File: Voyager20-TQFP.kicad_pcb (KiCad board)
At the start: 2 copper layers, 73 x 95.2 mm, 92 parts, among them Q1 Q_NPN_BEC, SW1 SW_Push, U1 ATmega32U2-AU, U2 PRTR5V0U2X, Y1 16MHz

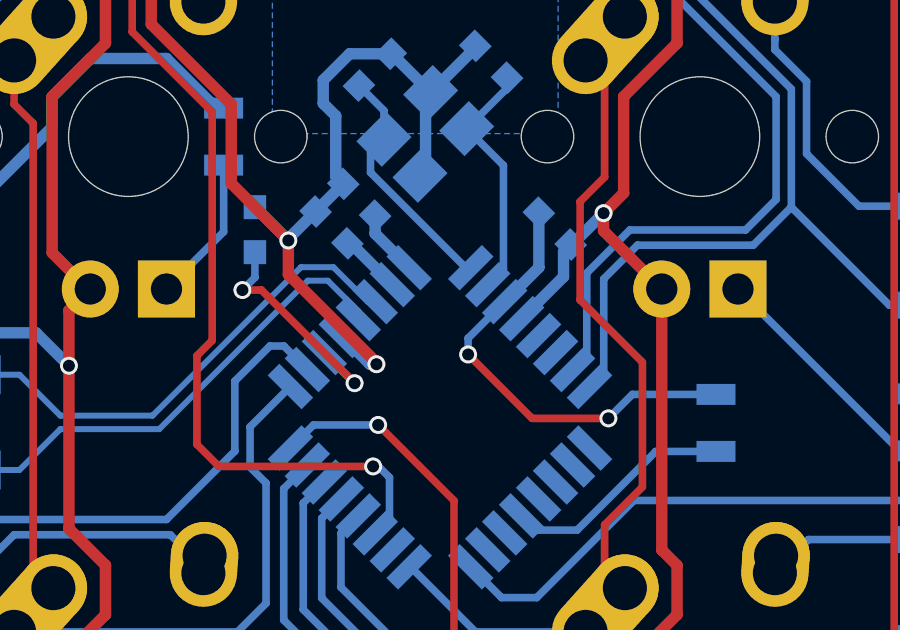
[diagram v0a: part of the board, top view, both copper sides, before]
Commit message: fixed +5v and GND lol
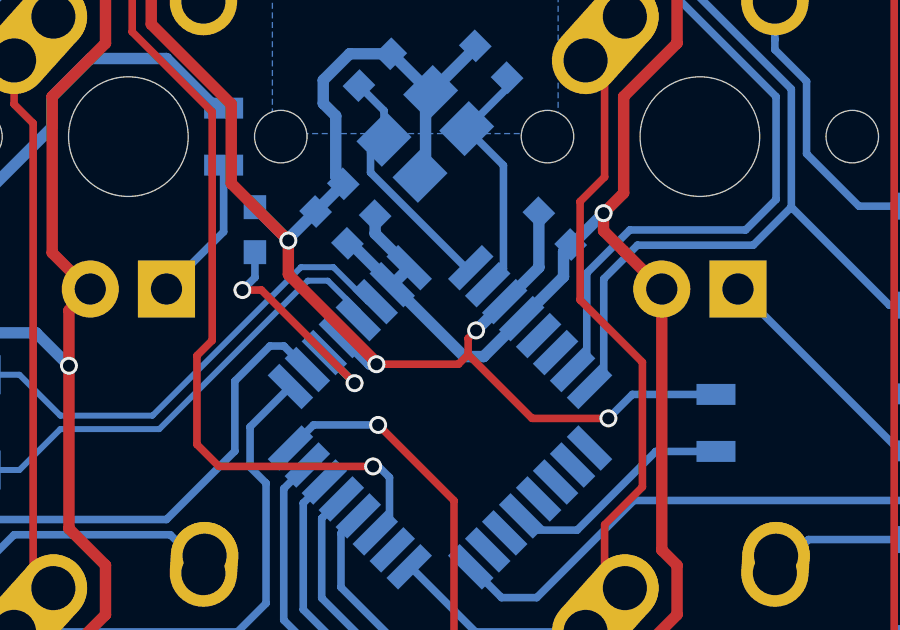
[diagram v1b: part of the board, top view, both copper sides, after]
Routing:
- net +5V: track 520.3 -> 526.9 mm
- net GND: track 312.8 -> 315.9 mm
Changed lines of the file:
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@@
   (segment (start 64.7555 33.7675) (end 61.47 33.7675) (width 0.381) (layer "F.Cu") (net 2))
   (segment (start 93.599 83.312) (end 93.599 98.298) (width 0.381) (layer "F.Cu") (net 2))
+  (segment (start 78 65.463578) (end 78.265949 65.197629) (width 0.254) (layer "F.Cu") (net 2))
   (segment (start 93.599 83.058) (end 93.726 83.185) (width 0.381) (layer "F.Cu") (net 2))
   (segment (start 92.583 101.346) (end 92.075 101.346) (width 0.381) (layer "F.Cu") (net 2))
@@
   (segment (start 52.324 41.402) (end 53.213 41.402) (width 0.381) (layer "F.Cu") (net 2))
   (segment (start 70.104 57.658) (end 67.437 54.991) (width 0.381) (layer "F.Cu") (net 2))
+  (segment (start 78 66) (end 78 65.463578) (width 0.254) (layer "F.Cu") (net 2))
   (segment (start 67.437 48.514) (end 69.596 46.355) (width 0.381) (layer "F.Cu") (net 2))
   (segment (start 93.599 73.66) (end 93.599 83.058) (width 0.381) (layer "F.Cu") (net 2))
   (segment (start 72.007097 62.200262) (end 70.104 60.297165) (width 0.381) (layer "F.Cu") (net 2))
   (segment (start 54.991 39.624) (end 59.309 39.624) (width 0.381) (layer "F.Cu") (net 2))
+  (segment (start 78 66) (end 77.676425 66.323575) (width 0.254) (layer "F.Cu") (net 2))
   (segment (start 90.043 103.378) (end 92.075 101.346) (width 0.381) (layer "F.Cu") (net 2))
+  (segment (start 77.676425 66.323575) (end 74.943604 66.323575) (width 0.254) (layer "F.Cu") (net 2))
   (segment (start 94.742 100.203) (end 93.599 101.346) (width 0.381) (layer "F.Cu") (net 2))
   (via (at 82.675481 68.129239) (size 0.6) (drill 0.4) (layers "F.Cu" "B.Cu") (net 2))
   (via (at 93.853 48.006) (size 0.6) (drill 0.4) (layers "F.Cu" "B.Cu") (net 2))
   (via (at 72.007097 62.200262) (size 0.6) (drill 0.4) (layers "F.Cu" "B.Cu") (net 2))
-  (via (at 78 66) (size 0.6) (drill 0.4) (layers "F.Cu" "B.Cu") (net 2))
   (via (at 93.726 83.185) (size 0.6) (drill 0.4) (layers "F.Cu" "B.Cu") (net 2))
   (via (at 52.324 41.402) (size 0.6) (drill 0.4) (layers "F.Cu" "B.Cu") (net 2))
   (via (at 59.309 39.624) (size 0.6) (drill 0.4) (layers "F.Cu" "B.Cu") (net 2))
+  (via (at 78.265949 65.197629) (size 0.6) (drill 0.4) (layers "F.Cu" "B.Cu") (net 2))
   (via (at 90.043 105.537) (size 0.6) (drill 0.4) (layers "F.Cu" "B.Cu") (net 2))
   (via (at 74.943604 66.323575) (size 0.6) (drill 0.4) (layers "F.Cu" "B.Cu") (net 2))
@@
   (segment (start 78.994 81.407) (end 80.899 81.407) (width 0.381) (layer "B.Cu") (net 2))
   (segment (start 76.581664 57.436867) (end 76.581664 59.841029) (width 0.381) (layer "B.Cu") (net 2))
+  (segment (start 79.218666 64.238712) (end 79.218666 64.244912) (width 0.381) (layer "B.Cu") (net 2))
   (segment (start 63.5 104.902) (end 59.944 101.346) (width 0.381) (layer "B.Cu") (net 2))
   (segment (start 59.055 39.878) (end 59.055 42.799) (width 0.381) (layer "B.Cu") (net 2))
@@
   (segment (start 90.60625 45.91875) (end 87.884 48.641) (width 0.381) (layer "B.Cu") (net 2))
   (segment (start 65.913 36.703) (end 65.913 34.925) (width 0.381) (layer "B.Cu") (net 2))
+  (segment (start 79.218666 64.244912) (end 78.265949 65.197629) (width 0.381) (layer "B.Cu") (net 2))
   (segment (start 65.913 34.925) (end 64.7555 33.7675) (width 0.381) (layer "B.Cu") (net 2))
   (segment (start 80.357879 63.099499) (end 80.357879 61.273772) (width 0.381) (layer "B.Cu") (net 2))
@@
   (segment (start 93.8125 47.66875) (end 92.0625 45.91875) (width 0.381) (layer "B.Cu") (net 2))
   (segment (start 78.238162 55.780369) (end 76.749693 57.268838) (width 0.381) (layer "B.Cu") (net 2))
-  (segment (start 78 65.457378) (end 78 66) (width 0.254) (layer "B.Cu") (net 2))
   (segment (start 80.899 81.407) (end 81.28 81.026) (width 0.381) (layer "B.Cu") (net 2))
   (segment (start 58.293 49.657) (end 57.1375 48.5015) (width 0.381) (layer "B.Cu") (net 2))
@@
   (segment (start 93.853 48.006) (end 93.853 47.70925) (width 0.381) (layer "B.Cu") (net 2))
   (segment (start 64.1865 105.6125) (end 63.5 105.6125) (width 0.381) (layer "B.Cu") (net 2))
-  (segment (start 79.218666 64.238712) (end 78 65.457378) (width 0.254) (layer "B.Cu") (net 2))
   (segment (start 61.47 33.7675) (end 61.47 29.5875) (width 0.381) (layer "B.Cu") (net 2))
   (segment (start 77.951774 58.470919) (end 79.298822 57.123871) (width 0.254) (layer "B.Cu") (net 3))
@@
   (segment (start 63.5 107.1125) (end 62.992 107.1125) (width 0.381) (layer "B.Cu") (net 5))
   (segment (start 65.405 44.7675) (end 65.405 45.974) (width 0.381) (layer "B.Cu") (net 5))
+  (segment (start 76.036685 63.107341) (end 75.471 63.673027) (width 0.381) (layer "B.Cu") (net 5))
   (segment (start 59.055 55.118) (end 53.721 55.118) (width 0.381) (layer "B.Cu") (net 5))
   (segment (start 88.9 107.1125) (end 93.04375 107.1125) (width 0.381) (layer "B.Cu") (net 5))
@@
   (segment (start 74.900047 61.970703) (end 76.036685 63.107341) (width 0.381) (layer "B.Cu") (net 5))
   (segment (start 81.468337 62.334432) (end 82.514333 61.288436) (width 0.381) (layer "B.Cu") (net 5))
+  (segment (start 77.867814 66.069841) (end 75.471 63.673027) (width 0.381) (layer "B.Cu") (net 5))
   (segment (start 45.085 46.101) (end 45.085 49.784) (width 0.381) (layer "B.Cu") (net 5))
   (segment (start 81.418539 62.334432) (end 81.468337 62.334432) (width 0.381) (layer "B.Cu") (net 5))
@@
   (segment (start 52.254 50.546) (end 52.3875 50.4125) (width 0.381) (layer "B.Cu") (net 5))
   (segment (start 53.721 55.118) (end 52.451 53.848) (width 0.381) (layer "B.Cu") (net 5))
+  (segment (start 79.784351 64.804397) (end 78.518907 66.069841) (width 0.381) (layer "B.Cu") (net 5))
   (segment (start 45.847 50.546) (end 52.254 50.546) (width 0.381) (layer "B.Cu") (net 5))
   (segment (start 100.31025 49.16875) (end 98.425 49.16875) (width 0.381) (layer "B.Cu") (net 5))
@@
   (segment (start 97.0125 49.16875) (end 95.2625 50.91875) (width 0.381) (layer "B.Cu") (net 5))
   (segment (start 88.9 107.1125) (end 88.1895 107.1125) (width 0.381) (layer "B.Cu") (net 5))
+  (segment (start 78.518907 66.069841) (end 77.867814 66.069841) (width 0.381) (layer "B.Cu") (net 5))
   (segment (start 66.802 47.371) (end 83.185 47.371) (width 0.381) (layer "B.Cu") (net 5))
   (segment (start 45.085 49.784) (end 45.847 50.546) (width 0.381) (layer "B.Cu") (net 5))
